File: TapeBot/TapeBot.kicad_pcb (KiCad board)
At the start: 2 copper layers, 152.4 x 101.6 mm, 0 parts

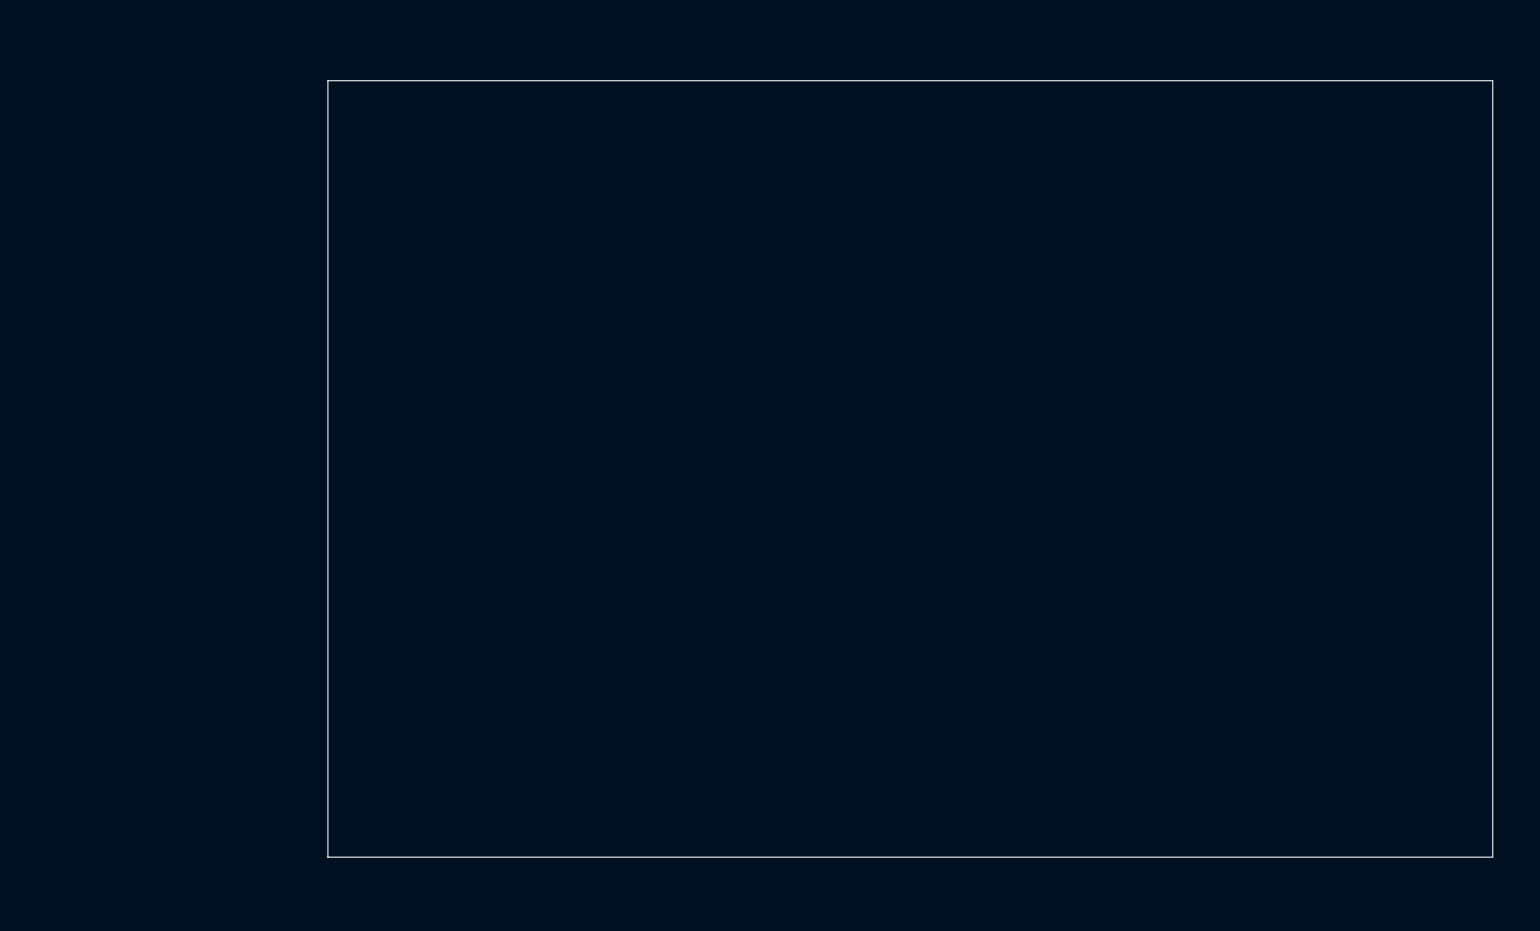
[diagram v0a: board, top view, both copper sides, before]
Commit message: fixed footprints and 3d models
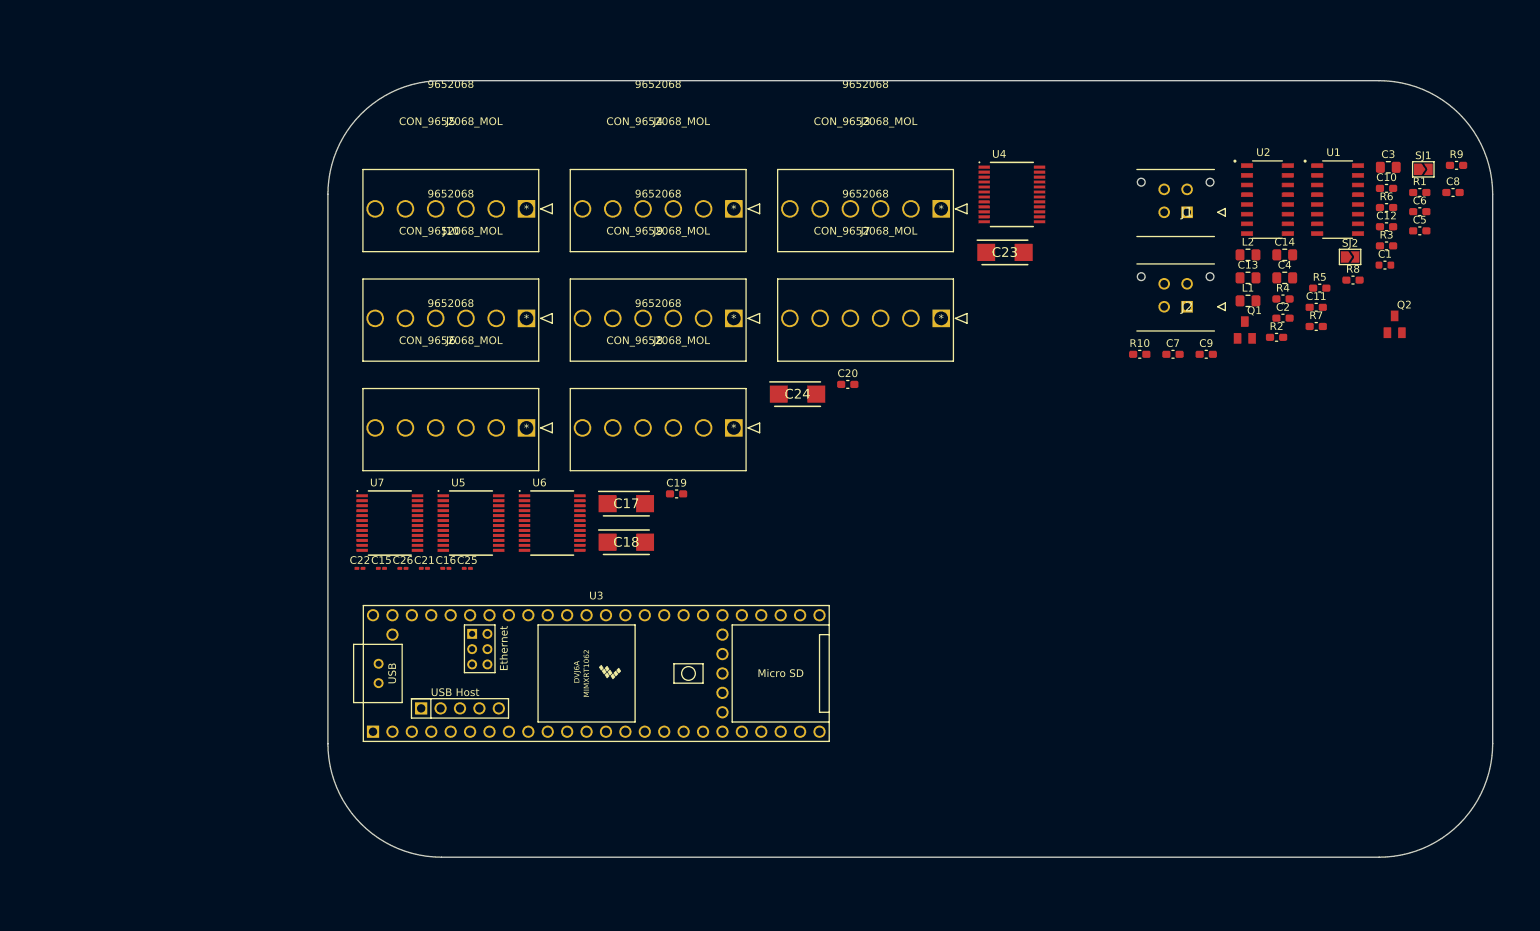
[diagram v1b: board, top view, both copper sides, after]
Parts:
- added C1: 0.1uF, Capacitor_SMD:C_0603_1608Metric, F.Cu at (222.4, 57.9)
- added C10: 0.1uF, Capacitor_SMD:C_0603_1608Metric_Pad1.08x0.95mm_HandSolder, F.Cu at (222.6, 47.9)
- added C11: 0.1uF, Capacitor_SMD:C_0603_1608Metric_Pad1.08x0.95mm_HandSolder, F.Cu at (213.4, 63.4)
- added C12: 0.1uF, Capacitor_SMD:C_0603_1608Metric_Pad1.08x0.95mm_HandSolder, F.Cu at (222.6, 52.9)
- added C13: 10uF, Capacitor_SMD:C_0805_2012Metric_Pad1.18x1.45mm_HandSolder, F.Cu at (204.5, 59.6)
- added C14: 10uF, Capacitor_SMD:C_0805_2012Metric_Pad1.18x1.45mm_HandSolder, F.Cu at (209.3, 56.6)
- added C15: 0.1uF, Capacitor_SMD:C_0201_0603Metric_Pad0.64x0.40mm_HandSolder, F.Cu at (91.1, 97.6)
- added C16: 0.1uF, Capacitor_SMD:C_0201_0603Metric_Pad0.64x0.40mm_HandSolder, F.Cu at (99.5, 97.6)
- added C17: 10uF, tapebot:CAPPM6032X280N, F.Cu at (123.1, 89.1)
- added C18: 10uF, tapebot:CAPPM6032X280N, F.Cu at (123.1, 94.2)
- added C19: 0.1uF, Capacitor_SMD:C_0603_1608Metric_Pad1.08x0.95mm_HandSolder, F.Cu at (129.7, 87.9)
- added C2: 0.1uF, Capacitor_SMD:C_0603_1608Metric_Pad1.08x0.95mm_HandSolder, F.Cu at (209.0, 64.9)
- added C20: 0.1uF, Capacitor_SMD:C_0603_1608Metric_Pad1.08x0.95mm_HandSolder, F.Cu at (152.1, 73.5)
- added C21: 0.1uF, Capacitor_SMD:C_0201_0603Metric_Pad0.64x0.40mm_HandSolder, F.Cu at (96.7, 97.6)
- added C22: 0.1uF, Capacitor_SMD:C_0201_0603Metric_Pad0.64x0.40mm_HandSolder, F.Cu at (88.3, 97.6)
- added C23: 10uF, tapebot:CAPPM6032X280N, F.Cu at (172.7, 56.3)
- added C24: 10uF, tapebot:CAPPM6032X280N, F.Cu at (145.5, 74.8)
- added C25: 0.1uF, Capacitor_SMD:C_0201_0603Metric_Pad0.64x0.40mm_HandSolder, F.Cu at (102.3, 97.6)
- added C26: 0.1uF, Capacitor_SMD:C_0201_0603Metric_Pad0.64x0.40mm_HandSolder, F.Cu at (93.9, 97.6)
- added C3: 10uF, Capacitor_SMD:C_0805_2012Metric_Pad1.18x1.45mm_HandSolder, F.Cu at (222.8, 45.1)
- added C4: 10uF, Capacitor_SMD:C_0805_2012Metric_Pad1.18x1.45mm_HandSolder, F.Cu at (209.3, 59.6)
- added C5: 0.1uF, Capacitor_SMD:C_0603_1608Metric_Pad1.08x0.95mm_HandSolder, F.Cu at (226.9, 53.4)
- added C6: 0.1uF, Capacitor_SMD:C_0603_1608Metric_Pad1.08x0.95mm_HandSolder, F.Cu at (226.9, 50.9)
- added C7: 0.1uF, Capacitor_SMD:C_0603_1608Metric_Pad1.08x0.95mm_HandSolder, F.Cu at (194.6, 69.6)
- added C8: 0.1uF, Capacitor_SMD:C_0603_1608Metric_Pad1.08x0.95mm_HandSolder, F.Cu at (231.3, 48.4)
- added C9: 0.1uF, Capacitor_SMD:C_0603_1608Metric_Pad1.08x0.95mm_HandSolder, F.Cu at (199.0, 69.6)
- added J1: 43045-0412, tapebot:43045-04YY_121314, F.Cu at (196.5, 51.0)
- added J10: CON_9652068_MOL, tapebot:9652068, F.Cu at (110.1, 64.9)
- added J2: 43045-0412, tapebot:43045-04YY_121314, F.Cu at (196.5, 63.4)
- added J3: CON_9652068_MOL, tapebot:9652068, F.Cu at (164.3, 50.6)
- added J4: CON_9652068_MOL, tapebot:9652068, F.Cu at (137.2, 50.6)
- added J5: CON_9652068_MOL, tapebot:9652068, F.Cu at (110.1, 50.6)
- added J6: CON_9652068_MOL, tapebot:9652068, F.Cu at (110.1, 79.2)
- added J7: CON_9652068_MOL, tapebot:9652068, F.Cu at (164.3, 64.9)
- added J8: CON_9652068_MOL, tapebot:9652068, F.Cu at (137.2, 79.2)
- added J9: CON_9652068_MOL, tapebot:9652068, F.Cu at (137.2, 64.9)
- added L1: 3.3uH, Capacitor_SMD:C_0805_2012Metric_Pad1.18x1.45mm_HandSolder, F.Cu at (204.5, 62.6)
- added L2: 3.3uH, Capacitor_SMD:C_0805_2012Metric_Pad1.18x1.45mm_HandSolder, F.Cu at (204.5, 56.6)
- added Q1: MMBT4403, tapebot:SOT23-BEC, F.Cu at (204.0, 66.4)
- added Q2: MMBT4403, tapebot:SOT23-BEC, F.Cu at (223.6, 65.7)
- added R1: 20k, Capacitor_SMD:C_0603_1608Metric_Pad1.08x0.95mm_HandSolder, F.Cu at (226.9, 48.4)
- added R10: 10K, Capacitor_SMD:C_0603_1608Metric_Pad1.08x0.95mm_HandSolder, F.Cu at (190.3, 69.6)
- added R2: 8.2K, Capacitor_SMD:C_0603_1608Metric_Pad1.08x0.95mm_HandSolder, F.Cu at (208.2, 67.4)
- added R3: 100, Capacitor_SMD:C_0603_1608Metric_Pad1.08x0.95mm_HandSolder, F.Cu at (222.6, 55.4)
- added R4: 100, Capacitor_SMD:C_0603_1608Metric_Pad1.08x0.95mm_HandSolder, F.Cu at (209.0, 62.3)
- added R5: 20k, Capacitor_SMD:C_0603_1608Metric_Pad1.08x0.95mm_HandSolder, F.Cu at (213.8, 60.9)
- added R6: 8.2K, Capacitor_SMD:C_0603_1608Metric_Pad1.08x0.95mm_HandSolder, F.Cu at (222.6, 50.4)
- added R7: 100, Capacitor_SMD:C_0603_1608Metric_Pad1.08x0.95mm_HandSolder, F.Cu at (213.4, 65.9)
- added R8: 100, Capacitor_SMD:C_0603_1608Metric_Pad1.08x0.95mm_HandSolder, F.Cu at (218.2, 59.9)
- added R9: 10K, Capacitor_SMD:C_0603_1608Metric_Pad1.08x0.95mm_HandSolder, F.Cu at (231.7, 44.9)
- added SJ1: JUMPER-PAD-2-NC_BY_TRACE, Jumper:SolderJumper-2_P1.3mm_Open_TrianglePad1.0x1.5mm, F.Cu at (227.4, 45.4)
- added SJ2: JUMPER-PAD-2-NC_BY_TRACE, Jumper:SolderJumper-2_P1.3mm_Open_TrianglePad1.0x1.5mm, F.Cu at (217.8, 56.8)
- added U1: HX711HX711, tapebot:SOP127P600X180-16N, F.Cu at (216.2, 49.3)
- added U2: HX711HX711, tapebot:SOP127P600X180-16N, F.Cu at (207.0, 49.3)
- added U3: Teensy4.1, teensy:Teensy41, F.Cu at (119.2, 111.3)
- added U4: TB6612FNG, tapebot:SOP65P760X160-24N, F.Cu at (173.6, 48.7)
- added U5: TB6612FNG, tapebot:SOP65P760X160-24N, F.Cu at (102.8, 91.7)
- added U6: TB6612FNG, tapebot:SOP65P760X160-24N, F.Cu at (113.4, 91.7)
- added U7: TB6612FNG, tapebot:SOP65P760X160-24N, F.Cu at (92.2, 91.7)
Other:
- outline, holes or cut-outs redrawn

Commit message: arranged board
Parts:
- added H1: MountingHole_Pad, MountingHole:MountingHole_4.3mm_M4_DIN965_Pad, F.Cu at (93.6, 43.3)
- added H2: MountingHole_Pad, MountingHole:MountingHole_4.3mm_M4_DIN965_Pad, F.Cu at (227.2, 43.3)
- added H3: MountingHole_Pad, MountingHole:MountingHole_4.3mm_M4_DIN965_Pad, F.Cu at (93.6, 126.2)
- added H4: MountingHole_Pad, MountingHole:MountingHole_4.3mm_M4_DIN965_Pad, F.Cu at (227.2, 126.6)
- C15, C16, C21, C22, C25, C26: footprint Capacitor_SMD:C_0201_0603Metric_Pad0.64x0.40mm_HandSolder -> Capacitor_SMD:C_0603_1608Metric_Pad1.08x0.95mm_HandSolder
- J10, J3, J4, J5, J6, J7, J8, J9: value CON_9652068_MOL -> 9652068
- moved C8 133.9 mm to (105.3, 93.9), turned to 180 degrees
- moved R6 126.2 mm to (103.3, 91.3)
- moved C1 124.2 mm to (98.2, 56.8), turned to -90 degrees
- moved C5 123.7 mm to (103.6, 63.1), turned to -90 degrees
- moved C3 123.2 mm to (100.2, 57.2), turned to -90 degrees
- moved R8 122.6 mm to (101.1, 96.0)
- moved C6 122.0 mm to (105.3, 60.3)
- moved R3 121.7 mm to (101.1, 62.2)
- moved Q2 121.2 mm to (104.0, 84.8), turned to 90 degrees
- moved R1 121.1 mm to (106.2, 57.0), turned to 90 degrees
- moved R7 116.7 mm to (101.1, 97.7)
- moved R9 115.9 mm to (116.5, 56.3)
- moved C2 113.6 mm to (98.2, 89.7), turned to 90 degrees
- moved C4 113.2 mm to (100.2, 89.9), turned to 90 degrees
- moved SJ1 111.9 mm to (116.3, 59.0), turned to 90 degrees
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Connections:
- C1 pad 1: /LoadCells/AVDD -> /LoadCells/AVDD1
- C17 pad A: (no net) -> +12V
- C17 pad C: (no net) -> GND
- C18 pad A: (no net) -> +12V
- C18 pad C: (no net) -> GND
- C2 pad 1: /LoadCells/AVDD -> /LoadCells/AVDD2
- C23 pad A: (no net) -> +12V
- C23 pad C: (no net) -> GND
- C24 pad A: (no net) -> +12V
- C24 pad C: (no net) -> GND
- C3 pad 1: /LoadCells/AVDD -> /LoadCells/AVDD1
- C4 pad 1: /LoadCells/AVDD -> /LoadCells/AVDD2
- J1 pad 1: /LoadCells/AVDD -> /LoadCells/AVDD1
- J1 pad 2: /LoadCells/A- -> /LoadCells/1A-
- J1 pad 4: /LoadCells/A+ -> /LoadCells/1A+
- J10 pad 2: /MotorDrivers/B02 -> /MotorDrivers/8B02
- J10 pad 3: /MotorDrivers/B01 -> /MotorDrivers/8B01
- J2 pad 1: /LoadCells/AVDD -> /LoadCells/AVDD2
- J2 pad 2: /LoadCells/A- -> /LoadCells/2A-
- J2 pad 4: /LoadCells/A+ -> /LoadCells/2A+
- J3 pad 2: /MotorDrivers/A02 -> /MotorDrivers/1A02
- J3 pad 3: /MotorDrivers/A01 -> /MotorDrivers/1A01
- J4 pad 2: /MotorDrivers/B02 -> /MotorDrivers/2B02
- J4 pad 3: /MotorDrivers/B01 -> /MotorDrivers/2B01
- J5 pad 2: /MotorDrivers/A02 -> /MotorDrivers/5A02
- J5 pad 3: /MotorDrivers/A01 -> /MotorDrivers/5A01
- J6 pad 2: /MotorDrivers/B02 -> /MotorDrivers/6B02
- J6 pad 3: /MotorDrivers/B01 -> /MotorDrivers/6B01
- J7 pad 2: /MotorDrivers/A02 -> /MotorDrivers/3A02
- J7 pad 3: /MotorDrivers/A01 -> /MotorDrivers/3A01
- J8 pad 2: /MotorDrivers/B02 -> /MotorDrivers/4B02
- J8 pad 3: /MotorDrivers/B01 -> /MotorDrivers/4B01
- J9 pad 2: /MotorDrivers/A02 -> /MotorDrivers/7A02
- J9 pad 3: /MotorDrivers/A01 -> /MotorDrivers/7A01
- L1 pad 1: /LoadCells/AVDD -> /LoadCells/AVDD1
- L2 pad 1: /LoadCells/AVDD -> /LoadCells/AVDD2
- R3 pad 1: /LoadCells/A- -> /LoadCells/1A-
- R4 pad 1: /LoadCells/A+ -> /LoadCells/1A+
- R7 pad 1: /LoadCells/A- -> /LoadCells/2A-
- R8 pad 1: /LoadCells/A+ -> /LoadCells/2A+
- U2 pad 11: L1_SCK -> L2_SCK
- U2 pad 12: L1_DAT -> L2_DAT
- U3 pad 12: M2_PWM -> M4_PWM
- U3 pad 13: M2_CTL1 -> M4_CTL1
- U3 pad 14: M2_CTL2 -> M4_CTL2
- U3 pad 16: L1_SCK -> L2_SCK
- U3 pad 19: M1_CTL2 -> M5_CTL2
- U3 pad 2: M2_CTL1 -> M8_CTL1
- U3 pad 20: M1_CTL1 -> M5_CTL1
- U3 pad 21: M1_PWM -> M5_PWM
- U3 pad 26: M1_CTL2 -> M7_CTL2
- U3 pad 27: M1_CTL1 -> M7_CTL1
- U3 pad 28: M1_PWM -> M7_PWM
- U3 pad 29: M2_PWM -> M6_PWM
- U3 pad 30: M2_CTL1 -> M6_CTL1
- U3 pad 31: M2_CTL2 -> M6_CTL2
- U3 pad 35: M2_PWM -> M8_PWM
- U3 pad 38: L1_DAT -> L2_DAT
- U3 pad 5: M2_CTL2 -> M8_CTL2
- U3 pad 6: M1_CTL2 -> M3_CTL2
- U3 pad 7: M1_CTL1 -> M3_CTL1
- U3 pad 8: M1_PWM -> M3_PWM
- U4 pad 1: /MotorDrivers/A01 -> /MotorDrivers/1A01
- U4 pad 11: /MotorDrivers/B01 -> /MotorDrivers/2B01
- U4 pad 12: /MotorDrivers/B01 -> /MotorDrivers/2B01
- U4 pad 2: /MotorDrivers/A01 -> /MotorDrivers/1A01
- U4 pad 5: /MotorDrivers/A02 -> /MotorDrivers/1A02
- U4 pad 6: /MotorDrivers/A02 -> /MotorDrivers/1A02
- U4 pad 7: /MotorDrivers/B02 -> /MotorDrivers/2B02
- U4 pad 8: /MotorDrivers/B02 -> /MotorDrivers/2B02
- U5 pad 1: /MotorDrivers/A01 -> /MotorDrivers/5A01
- U5 pad 11: /MotorDrivers/B01 -> /MotorDrivers/6B01
- U5 pad 12: /MotorDrivers/B01 -> /MotorDrivers/6B01
- U5 pad 15: M2_PWM -> M6_PWM
- U5 pad 16: M2_CTL2 -> M6_CTL2
- U5 pad 17: M2_CTL1 -> M6_CTL1
- U5 pad 2: /MotorDrivers/A01 -> /MotorDrivers/5A01
- U5 pad 21: M1_CTL1 -> M5_CTL1
- U5 pad 22: M1_CTL2 -> M5_CTL2
- U5 pad 23: M1_PWM -> M5_PWM
- U5 pad 5: /MotorDrivers/A02 -> /MotorDrivers/5A02
- U5 pad 6: /MotorDrivers/A02 -> /MotorDrivers/5A02
- U5 pad 7: /MotorDrivers/B02 -> /MotorDrivers/6B02
- U5 pad 8: /MotorDrivers/B02 -> /MotorDrivers/6B02
- U6 pad 1: /MotorDrivers/A01 -> /MotorDrivers/3A01
- U6 pad 11: /MotorDrivers/B01 -> /MotorDrivers/4B01
- U6 pad 12: /MotorDrivers/B01 -> /MotorDrivers/4B01
- U6 pad 15: M2_PWM -> M4_PWM
- U6 pad 16: M2_CTL2 -> M4_CTL2
- U6 pad 17: M2_CTL1 -> M4_CTL1
- U6 pad 2: /MotorDrivers/A01 -> /MotorDrivers/3A01
- U6 pad 21: M1_CTL1 -> M3_CTL1
- U6 pad 22: M1_CTL2 -> M3_CTL2
- U6 pad 23: M1_PWM -> M3_PWM
- U6 pad 5: /MotorDrivers/A02 -> /MotorDrivers/3A02
- U6 pad 6: /MotorDrivers/A02 -> /MotorDrivers/3A02
- U6 pad 7: /MotorDrivers/B02 -> /MotorDrivers/4B02
- U6 pad 8: /MotorDrivers/B02 -> /MotorDrivers/4B02
- U7 pad 1: /MotorDrivers/A01 -> /MotorDrivers/7A01
- U7 pad 11: /MotorDrivers/B01 -> /MotorDrivers/8B01
- U7 pad 12: /MotorDrivers/B01 -> /MotorDrivers/8B01
- U7 pad 15: M2_PWM -> M8_PWM
- U7 pad 16: M2_CTL2 -> M8_CTL2
- U7 pad 17: M2_CTL1 -> M8_CTL1
- U7 pad 2: /MotorDrivers/A01 -> /MotorDrivers/7A01
- U7 pad 21: M1_CTL1 -> M7_CTL1
- U7 pad 22: M1_CTL2 -> M7_CTL2
- U7 pad 23: M1_PWM -> M7_PWM
- U7 pad 5: /MotorDrivers/A02 -> /MotorDrivers/7A02
- U7 pad 6: /MotorDrivers/A02 -> /MotorDrivers/7A02
- U7 pad 7: /MotorDrivers/B02 -> /MotorDrivers/8B02
- U7 pad 8: /MotorDrivers/B02 -> /MotorDrivers/8B02
